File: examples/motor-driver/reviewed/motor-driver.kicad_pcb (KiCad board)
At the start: 2 copper layers, 88 x 50 mm, 12 parts, among them J1 VM 2.7-10.8V, J2 MOTOR A, J3 MOTOR B, J4 LOGIC, U1 DRV8833PW

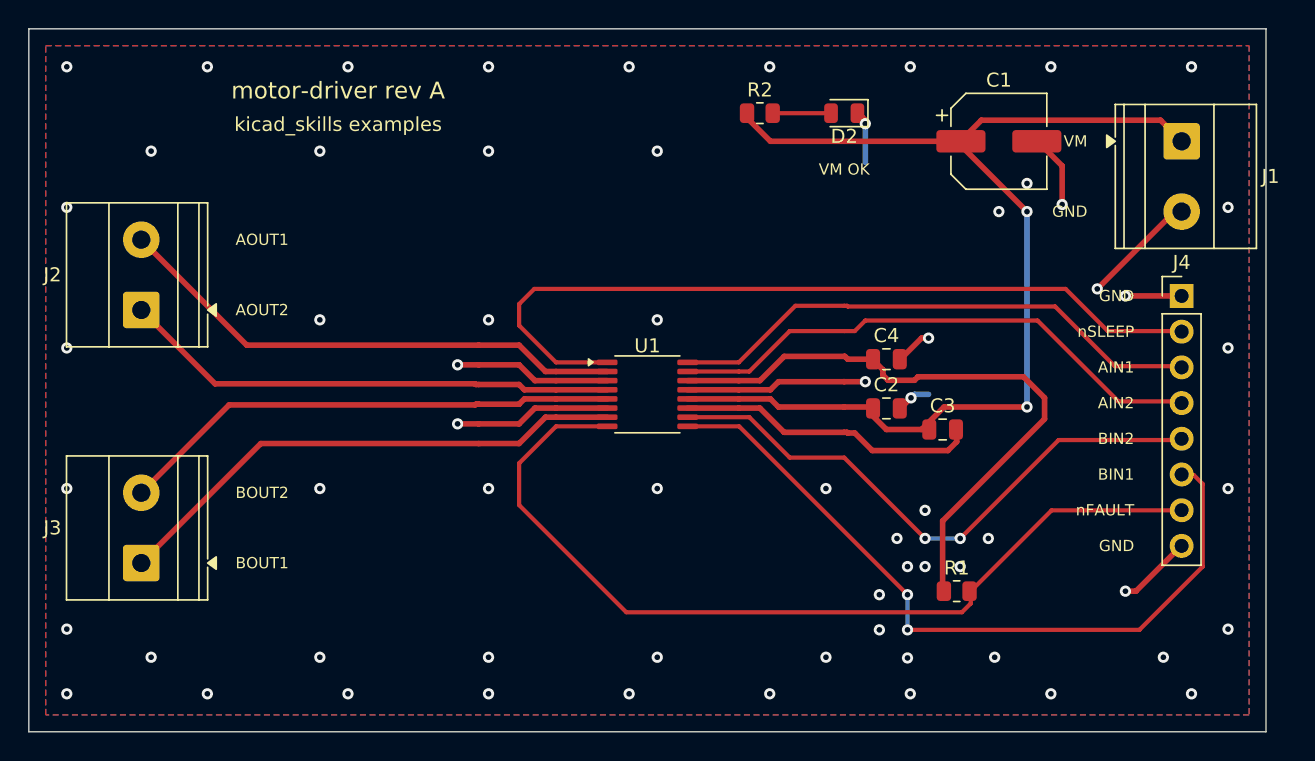
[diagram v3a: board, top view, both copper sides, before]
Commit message: Keep vias out of the lands they would drain
The reviewer's next one, and it is not one board's problem: vias were
landing inside surface-mount lands across the set. A hole in a land is a
hole solder wicks down during reflow - the joint above it starves, and
nothing on the assembled board tells that apart from a cold one.
Via-in-pad is a real technique and a filled-and-capped process, not a
drawing; a layout that has not specified the process may not draw it.

The router was the source. `_blocked` skips a route's own net, so
nothing stopped a layer change from happening on the very land the route
started at, and eighteen vias across three boards sat in one. Pads are
now marked as pads in the obstacle list and every one of them, whoever
owns it, is a cell where a via may not go - so an escape that has to
reach the plane leaves the land first and turns its via beside it. The
stitching pass kept ground vias a via-radius from ground lands where it
kept signal ones a radius plus clearance; both are the same distance
now, because the plane gains nothing from touching a land it can reach a
stub away.

`via.in_pad` measures the copper gap from every via to every land and
reports what is left. The exposed thermal pad under a package is exempt
- the via array in one is the datasheet's own answer, and nothing a
signal reaches is four square millimetres. It blocks under the
ai-generated policy: a generated board has no reason to draw this.

The test fixture had one too, a via twenty-five microns into C1's ground
land; it moves three tenths of a millimetre and the board is DRC clean
on both matrix versions as before.

Co-Authored-By: Claude Fable 5 <noreply@anthropic.com>
Claude-Session: https://claude.ai/code/session_01DUj7Ltu92tWg159mCSacwY
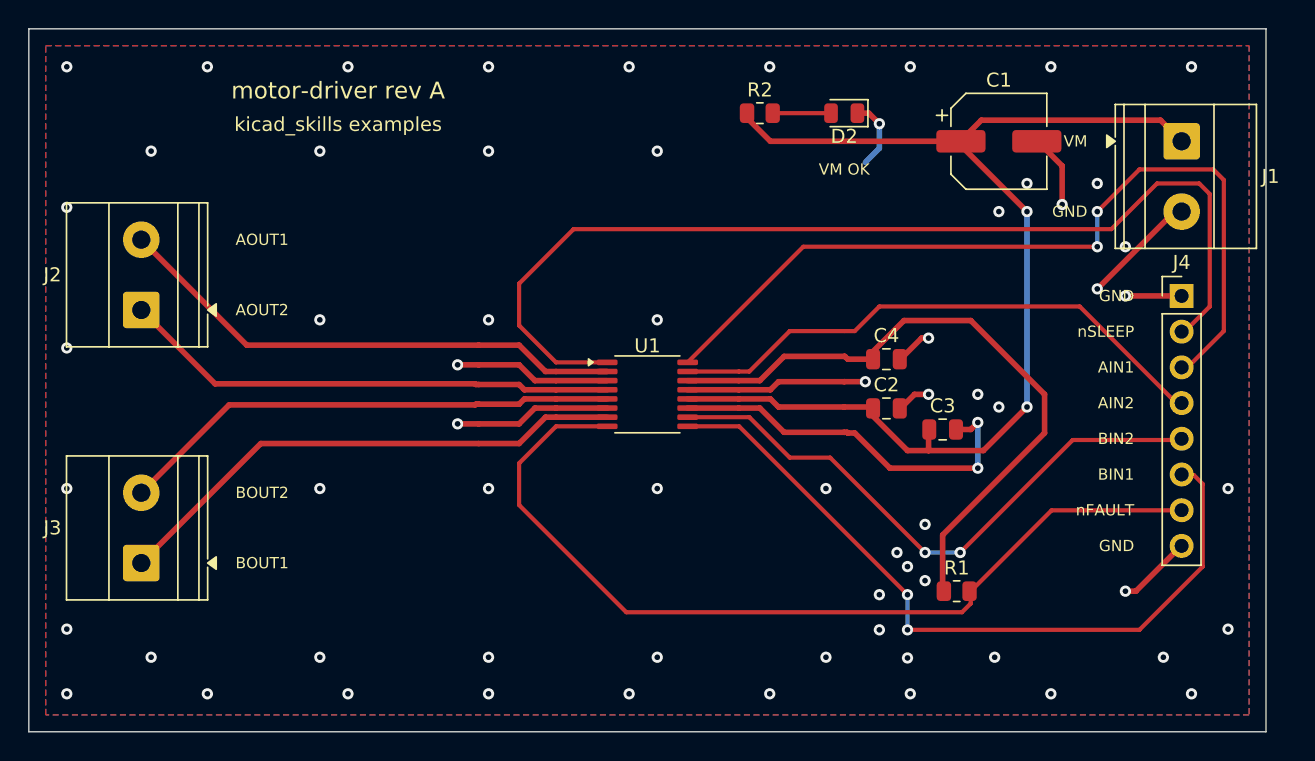
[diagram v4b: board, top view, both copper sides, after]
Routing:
- net /AIN1: track 38.6 -> 60.4 mm, vias 0 -> 2
- net /nSLEEP: track 57.7 -> 73.5 mm
- net /VCP: track 21.5 -> 27.4 mm, vias 0 -> 2
- net /VM: track 80.5 -> 83.0 mm
- net /VINT: track 44.6 -> 46.9 mm
- net GND: track 66.9 -> 68.1 mm
- net /BIN2: track 41.6 -> 42.5 mm
- net /AIN2: track 39.1 -> 39.9 mm

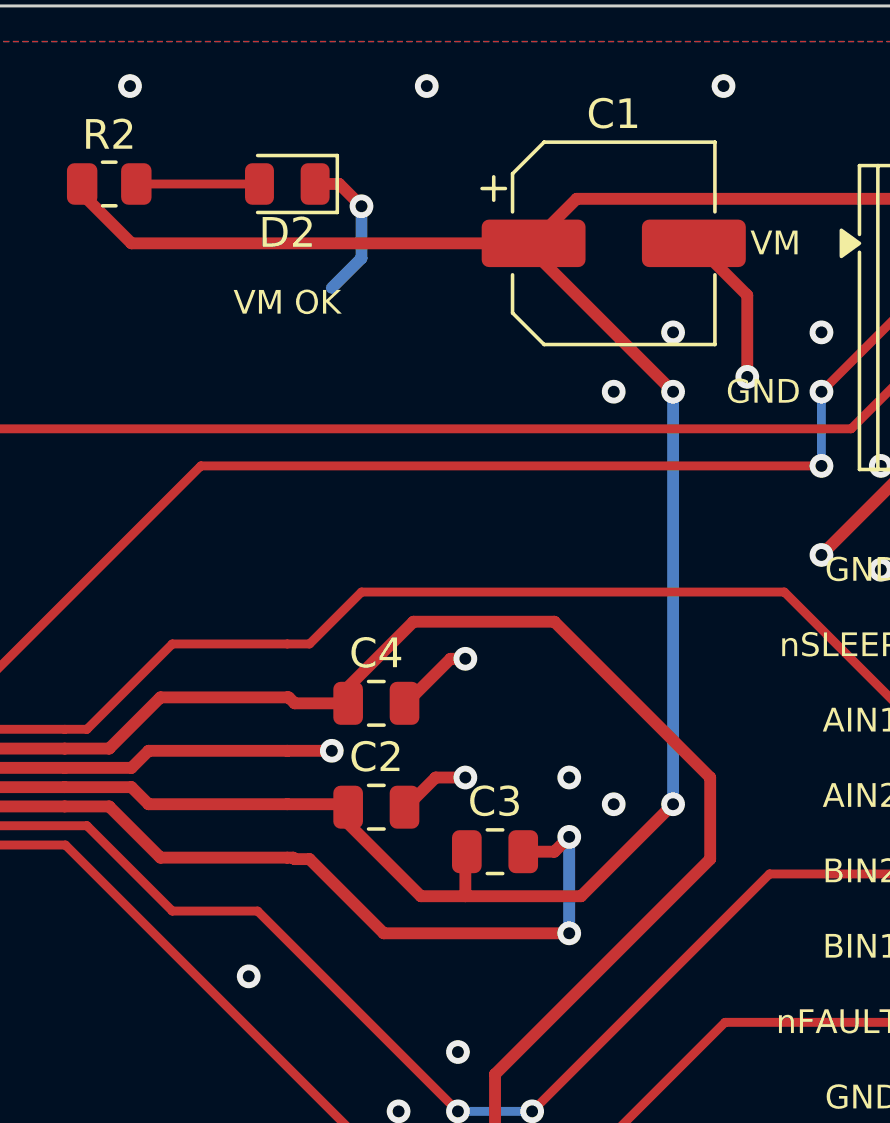
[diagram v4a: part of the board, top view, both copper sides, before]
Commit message: Give the vias room to stand beside the lands
Following the via-in-pad ban, the FPGA board stopped routing: five
attempts, five different nets, each one out of lanes in the corridor
between the FPGA's east escape fan and the codec's west one. Three
changes, in the order a layout would make them.

The via spacing was guesswork and is now the fab's. Hole to hole goes
from 1.2 mm to 0.9, which at the shipped 0.8/0.4 via leaves half a
millimetre of laminate between barrels - the ordinary minimum - and in a
1 mm-pitch escape comb is the difference between a lane and no lane.
What a via keeps off a land it may not sit in is its own radius plus a
solder-mask dam rather than the track clearance: the copper either side
may well be the same net, and what has to be true is that the mask can
part the barrel from the land.

Every decoupling capacitor now has its ground via placed against its own
pad rather than nine of them asking the search for one, and where the
via goes is chosen rather than fixed: `anchor_site` takes the nearest
position that clears everything already placed, fanning either side of
the direction facing off the part. A fixed offset walled off the
corridor its neighbour's supply needed - the via was legal, and it was
in the way.

And the seven parts sitting inside that corridor - four decoupling
capacitors, the two 1.2 V ones and the LED resistor - move four
millimetres south into the empty band below it. Twelve lanes leaving the
FPGA and ten arriving at the codec have eleven millimetres to cross in;
what a hand would do first is stop parking capacitors in the middle of
that, and it is the floorplan half of the debt this board's own README
has been carrying.

Co-Authored-By: Claude Fable 5 <noreply@anthropic.com>
Claude-Session: https://claude.ai/code/session_01DUj7Ltu92tWg159mCSacwY
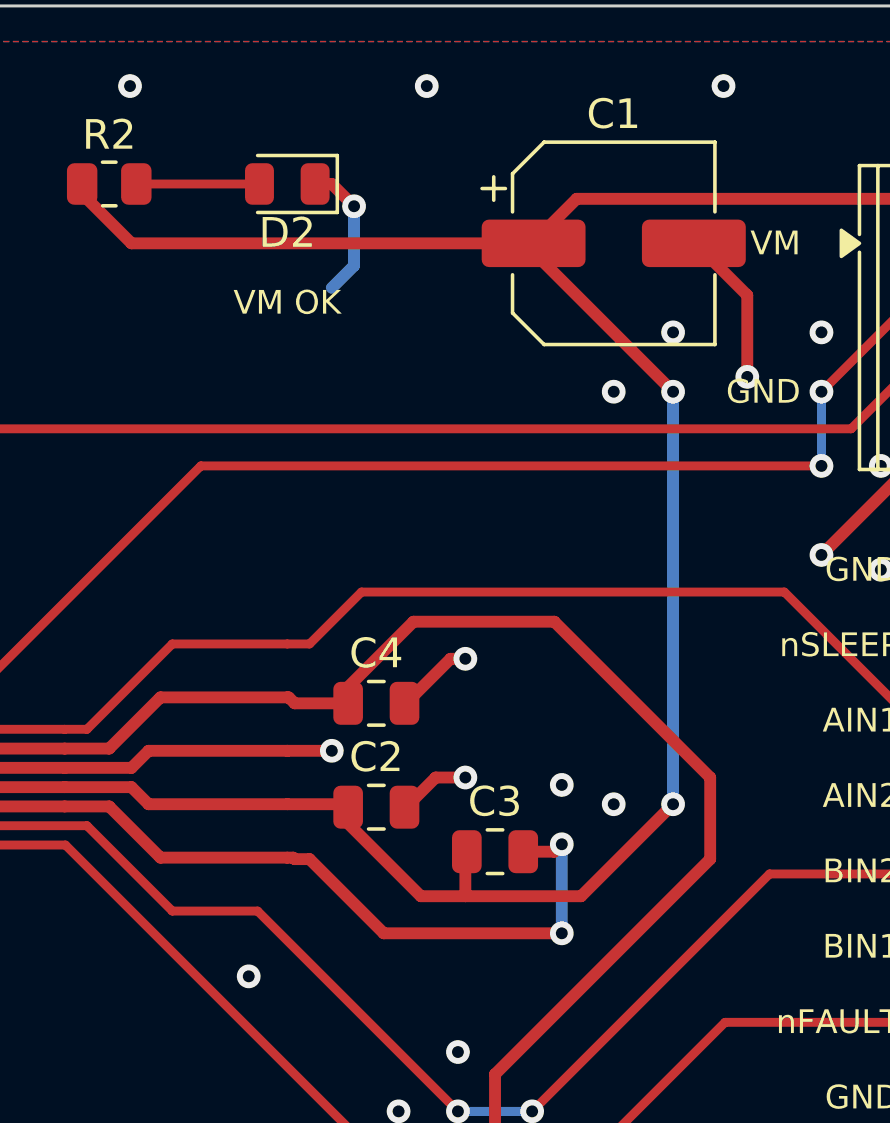
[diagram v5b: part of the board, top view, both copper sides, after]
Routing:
- net /VCP: track 27.4 -> 26.6 mm
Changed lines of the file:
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@@
 	(segment (start 181.75 97.0) (end 178.75 100.0) (width 0.4) (layer "F.Cu") (net 1))
 	(segment (start 178.75 100.0) (end 178.0 100.0) (width 0.4) (layer "F.Cu") (net 1))
-	(segment (start 158.9375 66.0) (end 159.75 66.0) (width 0.4) (layer "F.Cu") (net 1))
-	(segment (start 159.75 66.0) (end 160.5 66.75) (width 0.4) (layer "F.Cu") (net 1))
-	(segment (start 160.5 66.75) (end 160.5 68.5) (width 0.4) (layer "B.Cu") (net 1))
-	(segment (start 160.5 68.5) (end 159.5 69.5) (width 0.4) (layer "B.Cu") (net 1))
+	(segment (start 158.9375 66.0) (end 159.5 66.0) (width 0.4) (layer "F.Cu") (net 1))
+	(segment (start 159.5 66.0) (end 160.25 66.75) (width 0.4) (layer "F.Cu") (net 1))
+	(segment (start 160.25 66.75) (end 160.25 68.75) (width 0.4) (layer "B.Cu") (net 1))
+	(segment (start 160.25 68.75) (end 159.5 69.5) (width 0.4) (layer "B.Cu") (net 1))
 	(segment (start 141.1375 83.725) (end 137.5 83.725) (width 0.3) (layer "F.Cu") (net 15))
 	(segment (start 137.5 83.725) (end 134.875 81.1) (width 0.3) (layer "F.Cu") (net 15))
@@
 	(segment (start 158.25 88.75) (end 158.75 88.75) (width 0.4) (layer "F.Cu") (net 11))
 	(segment (start 158.75 88.75) (end 161.25 91.25) (width 0.4) (layer "F.Cu") (net 11))
-	(segment (start 161.25 91.25) (end 167.5 91.25) (width 0.4) (layer "F.Cu") (net 11))
+	(segment (start 161.25 91.25) (end 167.25 91.25) (width 0.4) (layer "F.Cu") (net 11))
 	(segment (start 146.8625 87.625) (end 151.25 87.625) (width 0.3) (layer "F.Cu") (net 7))
 	(segment (start 151.25 87.625) (end 154.125 90.5) (width 0.3) (layer "F.Cu") (net 7))
@@
 	(segment (start 151.0 66.25) (end 152.75 68.0) (width 0.4) (layer "F.Cu") (net 13))
 	(segment (start 152.75 68.0) (end 166.3 68.0) (width 0.4) (layer "F.Cu") (net 13))
-	(segment (start 167.5 91.25) (end 167.5 88.0) (width 0.4) (layer "B.Cu") (net 11))
-	(segment (start 167.5 88.0) (end 167.0 88.5) (width 0.4) (layer "F.Cu") (net 11))
+	(segment (start 167.25 91.25) (end 167.25 88.25) (width 0.4) (layer "B.Cu") (net 11))
+	(segment (start 167.25 88.25) (end 167.0 88.5) (width 0.4) (layer "F.Cu") (net 11))
 	(segment (start 167.0 88.5) (end 165.95 88.5) (width 0.4) (layer "F.Cu") (net 11))
 	(segment (start 152.9125 66.0) (end 157.0625 66.0) (width 0.3) (layer "F.Cu") (net 10))
@@
 	(via (at 164.0 82.0) (size 0.8) (drill 0.4) (layers "F.Cu" "B.Cu") (net 1))
 	(via (at 164.0 86.0) (size 0.8) (drill 0.4) (layers "F.Cu" "B.Cu") (net 1))
-	(via (at 167.5 91.25) (size 0.8) (drill 0.4) (layers "F.Cu" "B.Cu") (net 11))
-	(via (at 167.5 88.0) (size 0.8) (drill 0.4) (layers "F.Cu" "B.Cu") (net 11))
+	(via (at 167.25 91.25) (size 0.8) (drill 0.4) (layers "F.Cu" "B.Cu") (net 11))
+	(via (at 167.25 88.25) (size 0.8) (drill 0.4) (layers "F.Cu" "B.Cu") (net 11))
 	(via (at 173.5 72.5) (size 0.8) (drill 0.4) (layers "F.Cu" "B.Cu") (net 1))
 	(via (at 176.0 78.5) (size 0.8) (drill 0.4) (layers "F.Cu" "B.Cu") (net 1))
 	(via (at 178.0 79.0) (size 0.8) (drill 0.4) (layers "F.Cu" "B.Cu") (net 1))
 	(via (at 178.0 100.0) (size 0.8) (drill 0.4) (layers "F.Cu" "B.Cu") (net 1))
-	(via (at 160.5 66.75) (size 0.8) (drill 0.4) (layers "F.Cu" "B.Cu") (net 1))
+	(via (at 160.25 66.75) (size 0.8) (drill 0.4) (layers "F.Cu" "B.Cu") (net 1))
 	(via (at 176.0 75.5) (size 0.8) (drill 0.4) (layers "F.Cu" "B.Cu") (net 2))
 	(via (at 176.0 73.0) (size 0.8) (drill 0.4) (layers "F.Cu" "B.Cu") (net 2))
@@
 	(via (at 171.0 71.0) (size 0.8) (drill 0.4) (layers "F.Cu" "B.Cu") (net 1))
 	(via (at 169.0 86.9) (size 0.8) (drill 0.4) (layers "F.Cu" "B.Cu") (net 1))
-	(via (at 167.5 86.0) (size 0.8) (drill 0.4) (layers "F.Cu" "B.Cu") (net 1))
+	(via (at 167.25 86.25) (size 0.8) (drill 0.4) (layers "F.Cu" "B.Cu") (net 1))
 	(via (at 178.0 75.5) (size 0.8) (drill 0.4) (layers "F.Cu" "B.Cu") (net 1))
 	(via (at 176.0 71.0) (size 0.8) (drill 0.4) (layers "F.Cu" "B.Cu") (net 1))

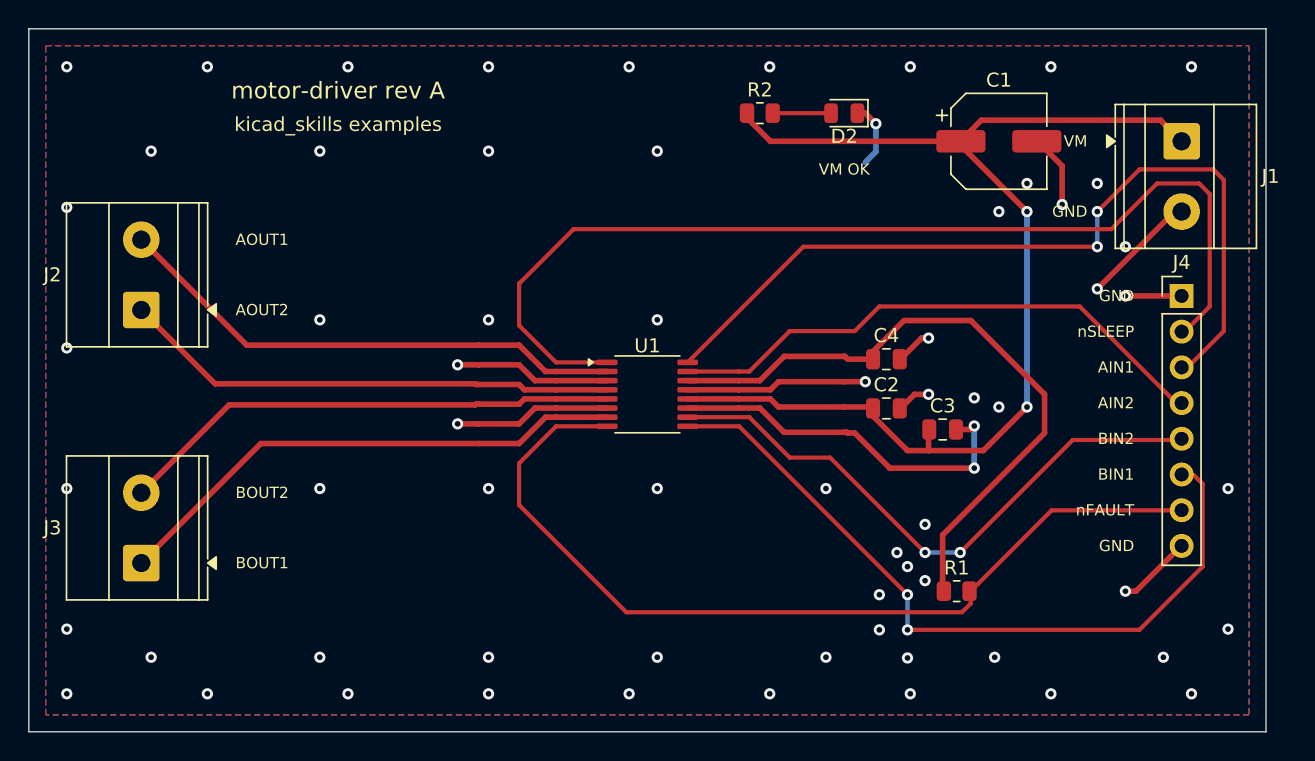
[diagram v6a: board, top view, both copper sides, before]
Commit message: Relieve the pads, fillet the joints, and give the board its screw holes
Three of the reviewer's manufacturing points, and they largely fall out
of the one before it - once KiCad fills the plane, the thermal relief it
was already asked for in the file actually appears.

**Thermal relief.** The zones said thermal all along; our own filler
ignored it and flooded every land solid. KiCad's does not, so every
through-hole ground pad now sits in a gap bridged by four spokes and an
iron can bring the joint up without heating a hundred square millimetres
of copper. `layout.solid_pad_connection` reports the setting when a
board turns it off: drilled pads only, because a surface pad reflows in
an oven that is heating the plane anyway and flooding it is often the
better thermal answer.

**Teardrops.** A track entering a land is a step change in width, and a
step change is where copper tears - the connector gets levered on and
off, the drill wanders, and the crack starts at the corner. `_teardrops`
replaces the first stretch of each run with a three-step taper into the
land, checked against its neighbours before it is kept, so a fillet
never eats the clearance a fine-pitch escape needs. It *replaces* rather
than overlays: laying the taper on top of the run drew the same copper
twice, and `route.acute_angle` reported all thirty of them, correctly.
`route.mixed_track_widths` learns what a fillet looks like so a properly
filleted board does not read as one nobody decided the width of.

**Mounting holes.** Four M3 holes near the corners, placed before the
router runs because they are obstacles, and slid along the edges or a
little inboard where a connector body has the corner - the motor board
and the op-amp take three, which is what those floorplans have room for.
Grounded on the motor driver, whose chassis is metal and part of the
shield, plain on the rest: bonding the enclosure to the reference is the
enclosure's decision, not the board's.

Two things that fell out of placing par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
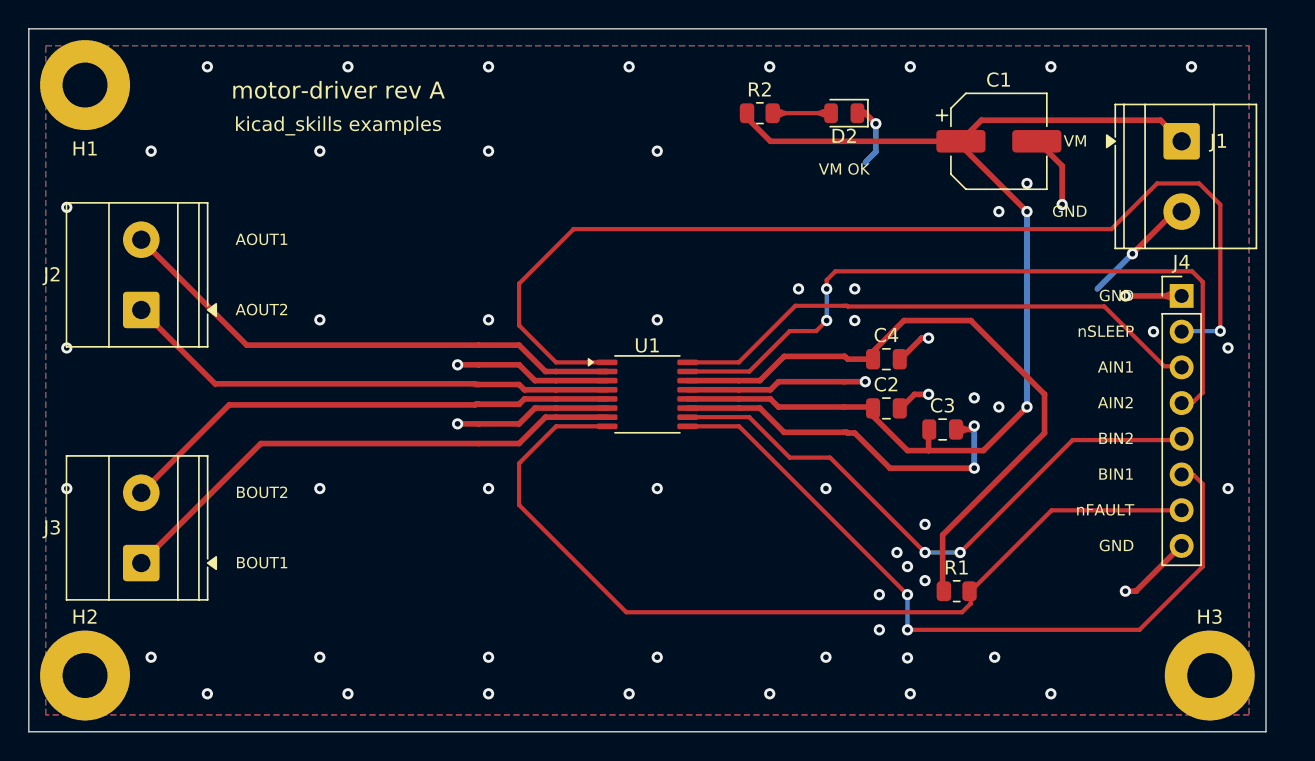
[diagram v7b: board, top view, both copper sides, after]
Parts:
- added H1: M33, MountingHole:MountingHole_3.2mm_M3_Pad, F.Cu at (104.0, 64.0)
- added H2: M33, MountingHole:MountingHole_3.2mm_M3_Pad, F.Cu at (104.0, 106.0)
- added H3: M33, MountingHole:MountingHole_3.2mm_M3_Pad, F.Cu at (184.0, 106.0)
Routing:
- net /AIN1: track 60.4 -> 38.6 mm, vias 2 -> 0
- net /AIN2: track 39.9 -> 51.3 mm, vias 0 -> 2
- net /nSLEEP: track 73.5 -> 75.5 mm, vias 0 -> 1
- net GND: vias 65 -> 62
